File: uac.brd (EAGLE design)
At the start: 100 x 100 mm, 222 parts, among them Q1 2N7002CK4SST, Q2 2N7002CK4SST, Q3 2N7002CK4SST, Q4 2N7002CK4SST, Q5 2N7002CK4SST, U1 MCP73833-FCI/UN, U2 ADXL345, Y1 RESONATORSMD

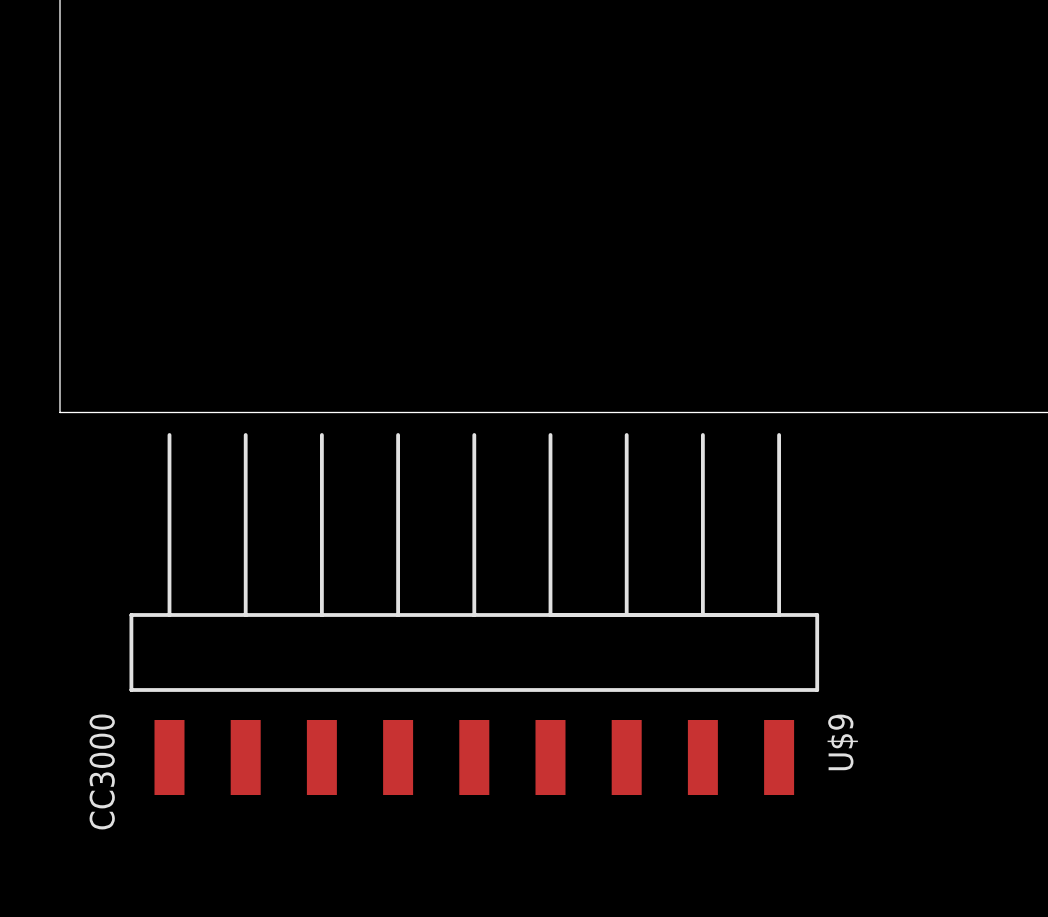
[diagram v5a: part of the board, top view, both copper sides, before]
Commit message: cc3300 on board
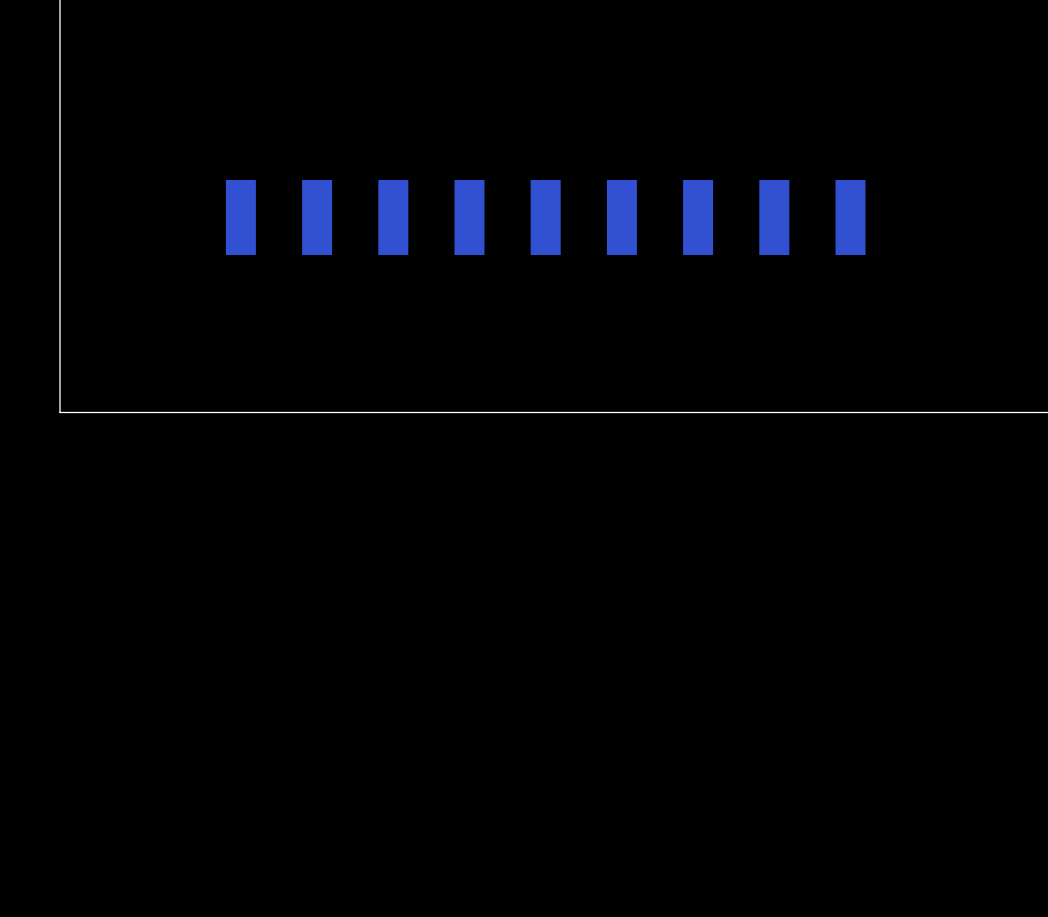
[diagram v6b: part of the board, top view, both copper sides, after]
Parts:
- moved U$9 20.6 mm to (20.0, 10.0), flipped to the bottom
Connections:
- net +3V3: now also U$9.3; no longer U$9.1
- net GND: now also U$9.1; no longer U$9.4
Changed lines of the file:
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@@
 <element name="R36" library="Custom components" package="R0603" value="10k" x="24.5" y="41.5" rot="MR180"/>
 <element name="R43" library="Custom components" package="R0603" value="10k" x="32.5" y="38.5" rot="MR90"/>
-<element name="U$2" library="timearc" package="CRYSTAL_32KHZ" value="CRYSTAL_32KHZ" x="75" y="55" rot="MR180"/>
+<element name="U$2" library="timearc" package="CRYSTAL_32KHZ" value="CRYSTAL_32KHZ" x="75" y="55" rot="MR180">
+<attribute name="MPN" value="MC-306 32.768K-E3:ROHS" x="75" y="55" size="1.778" layer="28" rot="MR180" display="off"/>
+<attribute name="OC_DIGIKEY_1" value="SER2417TR-ND" x="75" y="55" size="1.778" layer="28" rot="MR180" display="off"/>
+</element>
 <element name="C6" library="Custom components" package="C0603" value="100n" x="67" y="56.5" rot="MR90"/>
 <element name="C7" library="Custom components" package="C0603" value="100n" x="67" y="53" rot="MR90"/>
@@
 <element name="U$8" library="timearc" package="LED_5MM_SMD" value="LED_5MM_SMD" x="81.9" y="68.5" rot="MR60"/>
 <element name="R26" library="Custom components" package="R0603" value="200" x="85" y="66" rot="MR150"/>
-<element name="U$9" library="timearc" package="1X09-SMD" value="CC3000" x="10" y="-8"/>
+<element name="U$9" library="timearc" package="1X09-SMD" value="CC3000" x="20" y="10" rot="MR0"/>
 </elements>
 <signals>
@@
 <wire x1="81.272725" y1="75.427625" x2="82.8" y2="76.3" width="0.4064" layer="16"/>
 <via x="82.8" y="76.3" extent="1-16" drill="0.31"/>
-<contactref element="U$9" pad="4"/>
+<contactref element="U$9" pad="1"/>
 <wire x1="64.522375" y1="87.872721875" x2="81.272725" y2="75.427625" width="0" layer="19" extent="16-16"/>
 <wire x1="44" y1="90" x2="64.522375" y2="87.872721875" width="0" layer="19" extent="16-16"/>
@@
 <wire x1="92" y1="27" x2="93" y2="25" width="0" layer="19" extent="16-16"/>
 <wire x1="91.5" y1="48.35" x2="92" y2="33.3" width="0" layer="19" extent="16-16"/>
-<wire x1="8.73" y1="-11.5" x2="41" y2="18" width="0" layer="19" extent="1-1"/>
+<wire x1="26.35" y1="6.5" x2="41" y2="18" width="0" layer="19" extent="16-16"/>
 </signal>
 <signal name="+3V3">
@@
 <contactref element="C26" pad="1"/>
 <contactref element="C5" pad="1"/>
-<contactref element="U$9" pad="1"/>
+<contactref element="U$9" pad="3"/>
 <wire x1="65.85" y1="44.5" x2="91.5" y2="46.65" width="0" layer="19" extent="16-16"/>
 <wire x1="66" y1="40.65" x2="65.85" y2="44.5" width="0" layer="19" extent="16-16"/>
@@
 <wire x1="68.0988" y1="9" x2="61.901" y2="9" width="0" layer="19" extent="16-16"/>
 <wire x1="71" y1="9.15" x2="68.0988" y2="9" width="0" layer="19" extent="16-16"/>
-<wire x1="16.35" y1="-11.5" x2="58" y2="11.5" width="0" layer="19" extent="1-16"/>
+<wire x1="21.27" y1="6.5" x2="32.5" y2="37.65" width="0" layer="19" extent="16-16"/>
 </signal>
 <signal name="N$1">
@@
 <vertex x="88.5" y="16"/>
 </polygon>
+<wire x1="88.9906" y1="26.032" x2="90" y2="27" width="0" layer="19" extent="16-16"/>
+<wire x1="89" y1="29" x2="88.9906" y2="27.9906" width="0" layer="19" extent="16-16"/>
+<wire x1="90.5" y1="15.15" x2="89" y2="14" width="0" layer="19" extent="3-16"/>
+<wire x1="93" y1="15.15" x2="90.5" y2="15.15" width="0" layer="19" extent="16-16"/>
+<wire x1="93" y1="13.9" x2="93" y2="15.15" width="0" layer="19" extent="16-16"/>
 </signal>
 <signal name="N$21">
@@
 <vertex x="90.5" y="20"/>
 </polygon>
+<wire x1="88.508" y1="21.968" x2="88.9906" y2="21.968" width="0" layer="19" extent="16-16"/>
 </signal>
 <signal name="N$19">

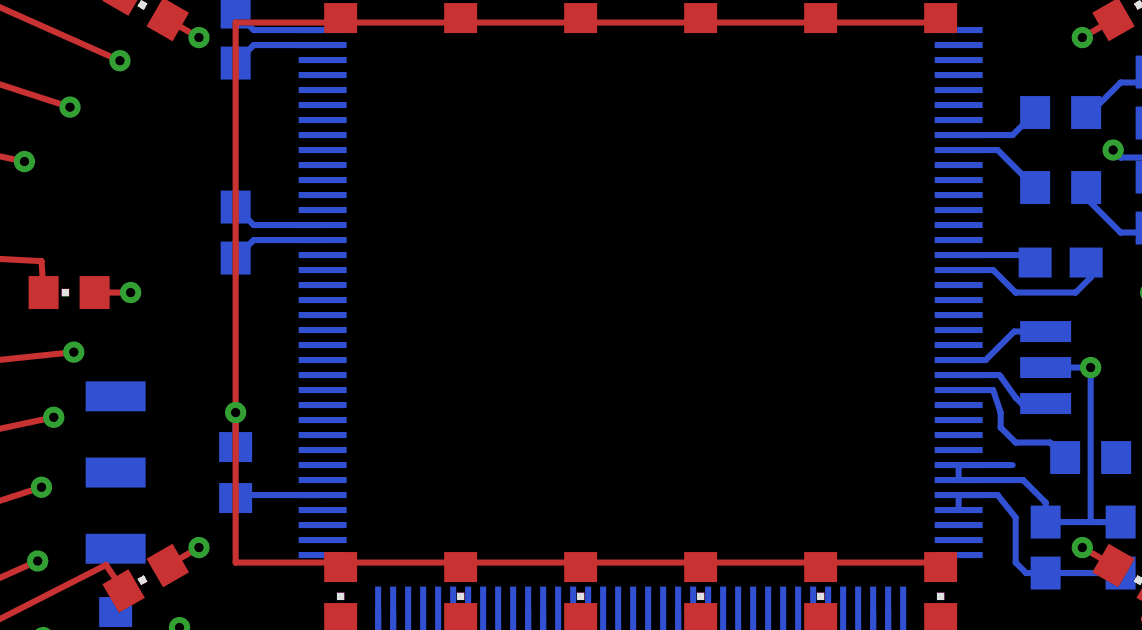
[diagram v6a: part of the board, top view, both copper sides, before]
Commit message: Light sensor added, wifi connected to spi2
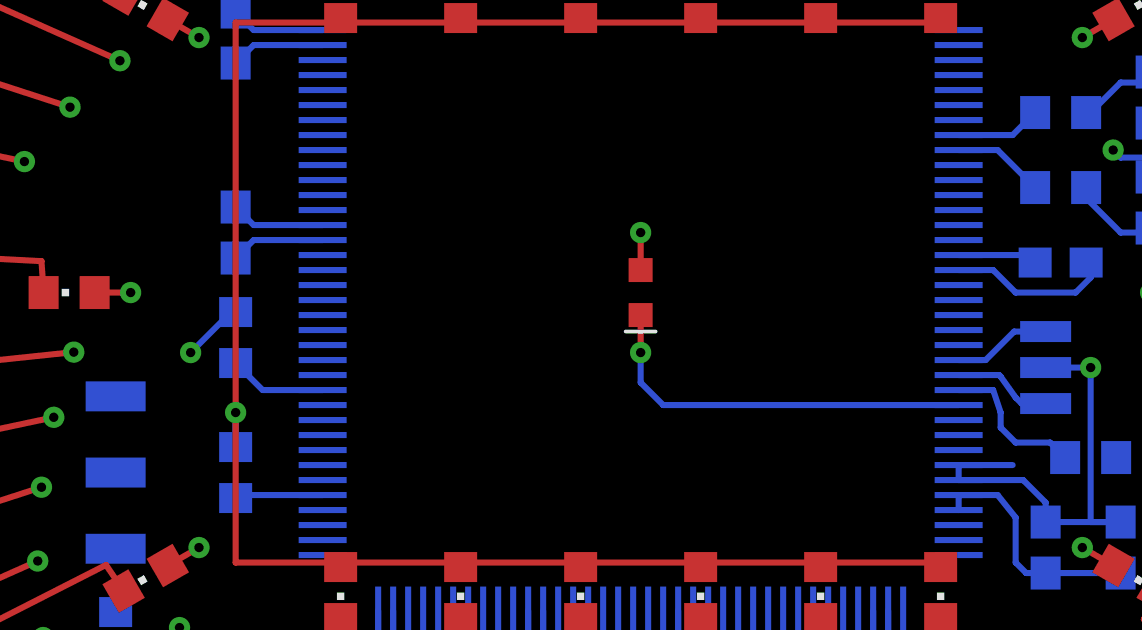
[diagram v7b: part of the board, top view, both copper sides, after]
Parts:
- added R27: 10k, Custom components:R0603
- added U$11: KDT0030, devergy_berkelaarmrt:FLD00030
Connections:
- new net LIGHT_SENSOR: R27.2, U$1.26, U$11.1
- new net SPI2_MISO: U$1.75, U$9.5
- new net SPI2_MOSI: U$1.76, U$9.4
- new net SPI2_NSS: U$1.73, U$9.6
- new net SPI2_SCK: U$1.74, U$9.8
- new net WIFI_EN: U$1.70, U$9.9
- new net WIFI_INT: U$1.69, U$9.7
- net +3V3: now also R27.1
- net GND: now also U$11.2
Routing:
- net LIGHT_SENSOR: track 0.00 -> 30.2 mm, vias 0 -> 2
- net +3V3: track 41.7 -> 45.0 mm
- net GND: track 76.3 -> 78.6 mm, vias 19 -> 20
